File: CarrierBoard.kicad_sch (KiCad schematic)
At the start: 4 parts

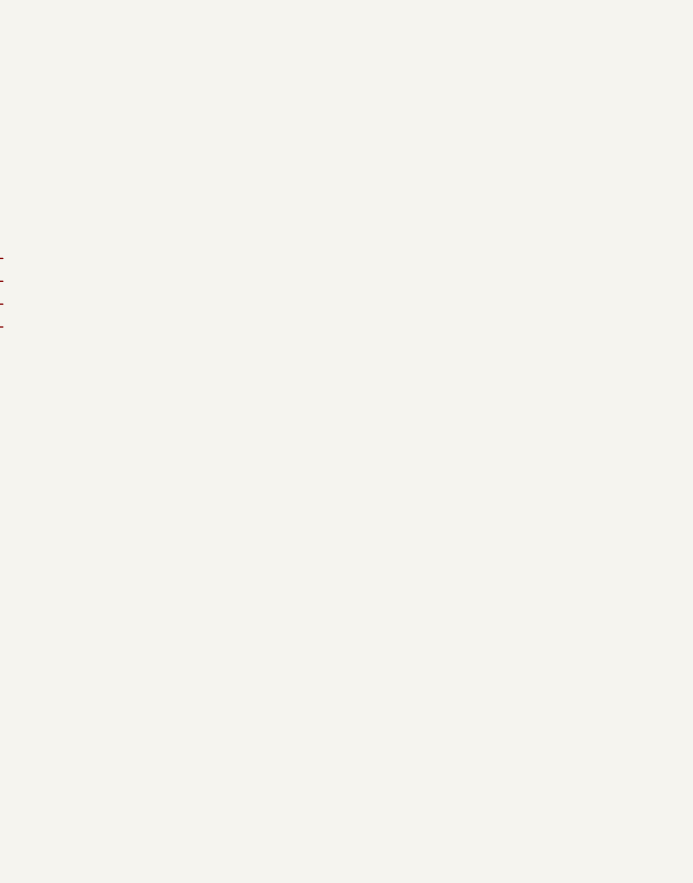
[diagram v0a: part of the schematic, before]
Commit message: added ESP32 Symbol
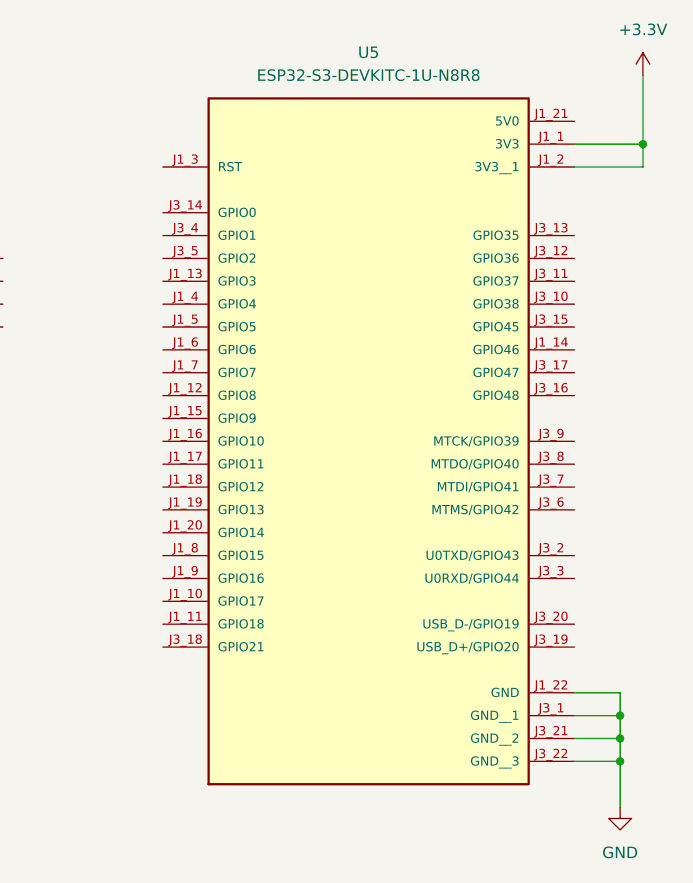
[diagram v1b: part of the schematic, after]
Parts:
- added U5: ESP32-S3-DEVKITC-1U-N8R8, ESP32-S3-DEVKITC-1U-N8R8:MODULE_ESP32-S3-DEVKITC-1U-N8R8, symbol ESP32-S3-DEVKITC-1U-N8R8:ESP32-S3-DEVKITC-1U-N8R8
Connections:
- net +3.3V: now also U5.J1_1 (3V3), U5.J1_2 (3V3__1)
- net GND: now also U5.J1_22 (GND), U5.J3_1 (GND__1), U5.J3_21 (GND__2), U5.J3_22 (GND__3)

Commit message: completed wiring
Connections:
- net GND: now also U2.5 (VIN-)
- net at U1.10 (ADR): now also U5.J1_7 (GPIO7)
- net at U1.4 (SDA): now also U5.J3_5 (GPIO2)
- net at U1.5 (SCL): now also U5.J3_4 (GPIO1)
- net at U1.6 (RST): now also U4.9 (RST), U5.J1_3 (RST)
- net at U1.7 (PS0): now also U5.J1_4 (GPIO4)
- net at U1.8 (PS1): now also U5.J1_5 (GPIO5)
- net at U1.9 (INT): now also U5.J1_6 (GPIO6)
- net at U2.3 (SCL): now also U5.J1_8 (GPIO15)
- net at U2.4 (SDA): now also U5.J1_9 (GPIO16)
- net at U3.3 (SDA): now also U5.J1_11 (GPIO18)
- net at U3.4 (SCL): now also U5.J3_18 (GPIO21)
- net at U5.J1_16 (GPIO10): now also U4.8 (CS)
- net at U5.J1_17 (GPIO11): now also U4.7 (MOSI)
- net at U5.J1_18 (GPIO12): now also U4.5 (SCK)
- net at U5.J1_19 (GPIO13): now also U4.6 (MISO)
- no-connect marks 0 -> 11
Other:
- note added: "Current Sensor"
- note added: "GNSS"
- note added: "IMU"
- note added: "LoRa"
- moved on the sheet: U1, U2, U3, U4, U5

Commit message: use 5v power, create bno footprint
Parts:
- U1: footprint (none) -> CarrierBoard:Untitled
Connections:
- net +3.3V: no longer U1.1 (Vin), U2.1 (VCC), U4.1 (VIN)
- net +5V: now reaches U5.J1_21 (5V0)
- net +5V: now also U1.1 (Vin), U2.1 (VCC), U4.1 (VIN)
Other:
- note added: "ESP32 powered by USB"

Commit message: most of layout, footprints
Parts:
- U1: footprint CarrierBoard:Untitled -> CarrierBoard:Adafruit BNO055
- U2: footprint (none) -> CarrierBoard:Adafruit INA219
- U3: footprint (none) -> CarrierBoard:SparkFun MAX-M10S
- U4: footprint (none) -> CarrierBoard:TE Connectivity 5-103639-8
- U5: footprint ESP32-S3-DEVKITC-1U-N8R8:MODULE_ESP32-S3-DEVKITC-1U-N8R8 -> CarrierBoard:ESP32-S3-DEVKITC-1U-N8R8
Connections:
- net at U3.4 (SCL): now also U5.J1_12 (GPIO8); no longer U5.J3_18 (GPIO21)
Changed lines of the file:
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@@
+	(wire
+		(pts
+			(xy 88.9 121.92) (xy 88.9 93.98)
+		)
+		(stroke
+			(width 0)
+			(type default)
+		)
+	)
 	(wire
 		(pts
@@
 	(wire
 		(pts
+			(xy 73.66 121.92) (xy 88.9 121.92)
+		)
+		(stroke
+			(width 0)
+			(type default)
+		)
+	)
+	(wire
+		(pts
 			(xy 76.2 149.86) (xy 76.2 147.32)
 		)
@@
 	(wire
 		(pts
+			(xy 88.9 93.98) (xy 93.98 93.98)
+		)
+		(stroke
+			(width 0)
+			(type default)
+		)
+	)
+	(wire
+		(pts
 			(xy 55.88 149.86) (xy 55.88 147.32)
 		)
@@
 		(pts
 			(xy 76.2 93.98) (xy 76.2 106.68)
-		)
-		(stroke
-			(width 0)
-			(type default)
-		)
-	)
-	(wire
-		(pts
-			(xy 73.66 121.92) (xy 93.98 121.92)
 		)
 		(stroke
@@
 			)
 		)
-		(property "Footprint" "CarrierBoard:Untitled"
+		(property "Footprint" "CarrierBoard:Adafruit BNO055"
 			(at 63.5 45.72 0)
 			(hide yes)
@@
 			)
 		)
-		(property "Footprint" ""
+		(property "Footprint" "CarrierBoard:Adafruit INA219"
 			(at 58.42 142.24 0)
 			(hide yes)
@@
 			)
 		)
-		(property "Footprint" ""
+		(property "Footprint" "CarrierBoard:SparkFun MAX-M10S"
 			(at 58.42 119.38 0)
 			(hide yes)
@@
 			)
 		)
-		(property "Footprint" "ESP32-S3-DEVKITC-1U-N8R8:MODULE_ESP32-S3-DEVKITC-1U-N8R8"
+		(property "Footprint" "CarrierBoard:ESP32-S3-DEVKITC-1U-N8R8"
 			(at 116.84 93.98 0)
 			(hide yes)
@@
 			)
 		)
-		(property "Footprint" ""
+		(property "Footprint" "CarrierBoard:TE Connectivity 5-103639-8"
 			(at 55.88 91.44 0)
 			(hide yes)

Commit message: redo board
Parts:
- removed U1: (no value), CarrierBoard:Adafruit BNO055, symbol CarrierBoard:Adafruit BNO055 MillMax Pins
- removed U2: (no value), CarrierBoard:Adafruit INA219, symbol CarrierBoard:Adafruit_INA219
- removed U3: (no value), CarrierBoard:SparkFun MAX-M10S, symbol CarrierBoard:SparkFun_GNSS_Receiver_MAX-M10S
- removed U4: (no value), CarrierBoard:TE Connectivity 5-103639-8, symbol CarrierBoard:Adafruit_RFM95W
- added U1: Adafruit RFM95W, internalcomponents:Adafruit RFM95W, symbol internalparts:Adafruit_RFM95W
- added U2: Adafruit INA-219, internalcomponents:INA-219 Adafruit Breakout, symbol internalparts:Adafruit_INA219
- added U3: SparkFun MAX-M10S, internalcomponents:MAX-M10S Sparkfun Breakout, symbol internalparts:SparkFun_MAX-M10S
- added U6: Adafruit BNO-055, CarrierBoard:Adafruit BNO055, symbol internalparts:Adafruit_BNO055
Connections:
- net +3.3V: now also U2.1 (VCC), U3.12 (3V3), U3.16 (3V3), U3.2 (3V3), U6.1 (V_{in})
- net +5V: now also U1.1 (V_{in})
- net GND: now also U1.2 (GND), U2.2 (GND), U2.5 (VIN-), U3.1 (GND), U3.14 (GND), U3.15 (GND), U6.3 (GND)
- net GYRO_INT: now reaches U5.J3_4 (GPIO1)
- net GYRO_INT: now also U6.9 (INT)
- net I2C0_SCL: now reaches U5.J1_11 (GPIO18)
- net I2C0_SCL: now also U6.5 (SCL)
- net I2C0_SDA: now reaches U5.J1_10 (GPIO17)
- net I2C0_SDA: now also U6.4 (SDA)
- net SPI2_CS: now reaches U5.J1_16 (GPIO10)
- net SPI2_CS: now also U1.8 (CS)
- net SPI2_MOSI: now reaches U5.J1_17 (GPIO11)
- net SPI2_MOSI: now also U1.7 (MOSI)
- net SPI2_SCK: now reaches U5.J1_18 (GPIO12)
- net SPI2_SCK: now also U1.5 (SCK)
- net SPI2_MISO: now reaches U5.J1_19 (GPIO13)
- net SPI2_MISO: now also U1.6 (MISO)
- net I2C1_SCL: now reaches U5.J3_16 (GPIO48)
- net I2C1_SCL: now also U2.3 (SCL), U3.17 (SDA)
- net I2C1_SDA: now reaches U5.J3_17 (GPIO47)
- net I2C1_SDA: now also U2.4 (SDA), U3.18 (SCL)
- new net: U3.10 (TX), U3.4 (TX)
- new net: U3.11 (RX), U3.5 (RX)
- no-connect marks 11 -> 44
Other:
- note added: "Core"
- note added: "Current/Voltage Sensor"
- note added: "GPS"
- note added: "I2C# | Device | Addresses ------------------------------------------------------ I2C 0 | BNO-055 IMU | [0x29], 0x28 I2C 1 | MAX-M10S GPS | [0x42] I2C 1 | INA-219 V/I Sens. | [0x40], 0x41, 0x44, 0x45"
- note added: "Inertial Measurement Unit"
- note added: "LoRA"
- note added: "Quick Facts: I2C0: GPIO1-2 I2C1: GPIO16-17 SPI2: GPIO10-13"
- note added: "URC Super Intelligence"
- note removed: "Current Sensor"
- note removed: "ESP32 powered by USB"
- note removed: "GNSS"
- note removed: "IMU"
- note removed: "LoRa"
- moved on the sheet: U5
